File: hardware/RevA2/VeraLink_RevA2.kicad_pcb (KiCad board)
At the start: 2 copper layers, 42 x 42 mm, 55 parts, among them J1 MAG_POGO_3PIN, J2 FACTORY_SWD_PADS, M1 COIN_LRA_MOTOR, SW1 USER_BUTTON, U1 MCP73831-2-OT, U2 TPS78233DDC, U3 nRF52840-QIAA, U4 E22-900M22S_SX1262_LORA, U5 DRV2605LDGS, Y1 32MHz, Y2 32.768 kHZ

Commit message: Apply Rev A2 layout repair pass 2
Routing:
- net Net-(U3-XL2/P0.01): track 3.57 -> 0.00 mm
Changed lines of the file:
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@@
-	)
-	(segment
-		(start 130.5 109.898959)
-		(end 130.5 109.75)
-		(width 0.2)
-		(layer "F.Cu")
-		(net "Net-(U3-XL2{slash}P0.01)")
-	)
-	(segment
-		(start 131.4 112.8)
-		(end 130.325 111.725)
-		(width 0.2)
-		(layer "F.Cu")
-		(net "Net-(U3-XL2{slash}P0.01)")
-	)
-	(segment
-		(start 130.325 111.725)
-		(end 130.325 110.073959)
-		(width 0.2)
-		(layer "F.Cu")
-		(net "Net-(U3-XL2{slash}P0.01)")
-	)
-	(segment
-		(start 130.325 110.073959)
-		(end 130.5 109.898959)
-		(width 0.2)
-		(layer "F.Cu")
-		(net "Net-(U3-XL2{slash}P0.01)")
 	)
 	(segment
@@
 	)
 	(segment
-		(start 130 109.75)
-		(end 129.601041 109.75)
-		(width 0.2)
-		(layer "F.Cu")
-		(net "Net-(U3-XL1{slash}P0.00)")
-	)
-	(segment

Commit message: Set Rev A2 PCB to 4-layer stackup
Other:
- copper layers 2 -> 4
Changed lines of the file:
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@@
 	(layers
 		(0 "F.Cu" signal)
+		(4 "In1.Cu" signal)
+		(6 "In2.Cu" signal)
 		(2 "B.Cu" signal)
 		(9 "F.Adhes" user "F.Adhesive")
@@
 	)
 	(setup
+		(stackup
+			(layer "F.SilkS"
+				(type "Top Silk Screen")
+			)
+			(layer "F.Paste"
+				(type "Top Solder Paste")
+			)
+			(layer "F.Mask"
+				(type "Top Solder Mask")
+				(thickness 0.01)
+			)
+			(layer "F.Cu"
+				(type "copper")
+				(thickness 0.035)
+			)
+			(layer "dielectric 1"
+				(type "prepreg")
+				(thickness 0.1)
+				(material "FR4")
+				(epsilon_r 4.5)
+				(loss_tangent 0.02)
+			)
+			(layer "In1.Cu"
+				(type "copper")
+				(thickness 0.035)
+			)
+			(layer "dielectric 2"
+				(type "core")
+				(thickness 1.24)
+				(material "FR4")
+				(epsilon_r 4.5)
+				(loss_tangent 0.02)
+			)
+			(layer "In2.Cu"
+				(type "copper")
+				(thickness 0.035)
+			)
+			(layer "dielectric 3"
+				(type "prepreg")
+				(thickness 0.1)
+				(material "FR4")
+				(epsilon_r 4.5)
+				(loss_tangent 0.02)
+			)
+			(layer "B.Cu"
+				(type "copper")
+				(thickness 0.035)
+			)
+			(layer "B.Mask"
+				(type "Bottom Solder Mask")
+				(thickness 0.01)
+			)
+			(layer "B.Paste"
+				(type "Bottom Solder Paste")
+			)
+			(layer "B.SilkS"
+				(type "Bottom Silk Screen")
+			)
+			(copper_finish "None")
+			(dielectric_constraints no)
+		)
 		(pad_to_mask_clearance 0)
 		(allow_soldermask_bridges_in_footprints no)
@@
 		(capping no)
 		(filling no)
+		(zone_defaults)
 		(pcbplotparams
 			(layerselection 0x00000000_00000000_55555555_5755f5ff)

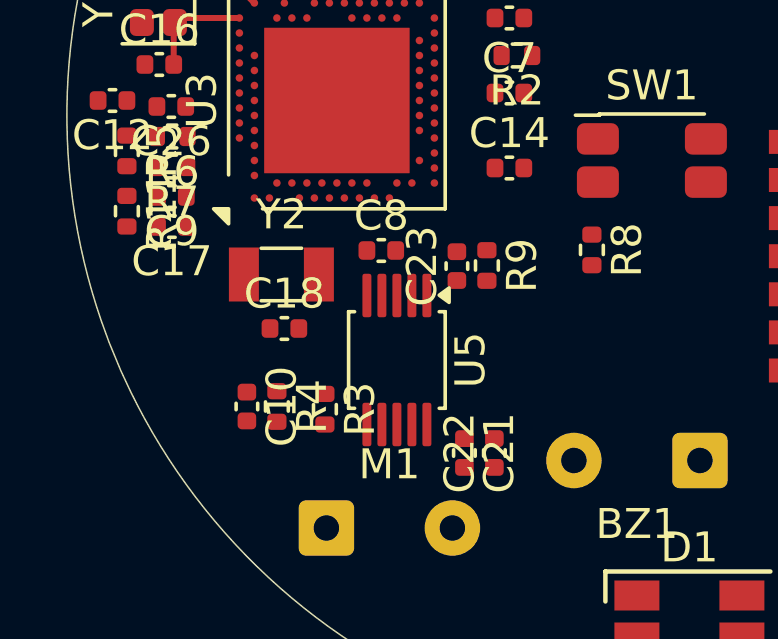
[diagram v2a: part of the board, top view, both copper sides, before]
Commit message: Route Rev A2 low frequency crystal nets
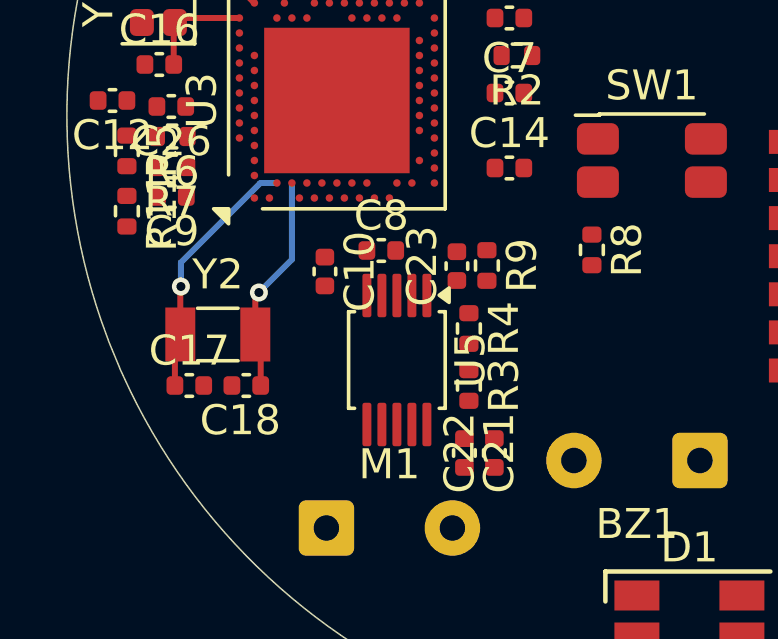
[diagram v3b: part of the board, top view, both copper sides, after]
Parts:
- moved R4 6.91 mm to (136.4, 114.6)
- moved C17 5.33 mm to (127.1, 116.5), turned to 0 degrees
- moved C10 5.20 mm to (131.6, 112.7)
- moved R3 4.86 mm to (136.4, 116.5)
- moved Y2 2.91 mm to (128.0, 114.8)
- moved C18 2.29 mm to (129.0, 116.5), turned to 180 degrees
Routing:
- net Net-(U3-XL1/P0.00): track 0.00 -> 8.48 mm, vias 0 -> 1
- net Net-(U3-XL2/P0.01): track 0.00 -> 7.33 mm, vias 0 -> 1
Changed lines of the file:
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@@
 		(capping no)
 		(filling no)
-		(zone_defaults)
 		(pcbplotparams
 			(layerselection 0x00000000_00000000_55555555_5755f5ff)
@@
 	(footprint "Resistor_SMD:R_0402_1005Metric"
 		(layer "F.Cu")
-		(at 130 117.2 -90)
+		(at 136.4 114.6 -90)
 		(descr "Resistor SMD 0402 (1005 Metric), square (rectangular) end terminal, IPC-7351 nominal, (Body size source: IPC-SM-782 page 72, https://www.pcb-3d.com/wordpress/wp-content/uploads/ipc-sm-782a_amendment_1_and_2.pdf)")
 		(tags "resistor")
@@
 	(footprint "Capacitor_SMD:C_0402_1005Metric"
 		(layer "F.Cu")
-		(at 130.25 114.6)
+		(at 128.98 116.5 180)
 		(descr "Capacitor SMD 0402 (1005 Metric), square (rectangular) end terminal, IPC-7351 nominal, (Body size source: IPC-SM-782 page 76, https://www.pcb-3d.com/wordpress/wp-content/uploads/ipc-sm-782a_amendment_1_and_2.pdf)")
 		(tags "capacitor")
 		(property "Reference" "C18"
-			(at 0 -1.16 0)
+			(at 0.2 -1.16 0)
 			(layer "F.SilkS")
 			(effects
@@
 		(duplicate_pad_numbers_are_jumpers no)
 		(fp_line
-			(start -0.107836 -0.36)
-			(end 0.107836 -0.36)
+			(start -0.107836 0.36)
+			(end 0.107836 0.36)
 			(stroke
 				(width 0.12)
@@
 		)
 		(fp_line
-			(start -0.107836 0.36)
-			(end 0.107836 0.36)
+			(start -0.107836 -0.36)
+			(end 0.107836 -0.36)
 			(stroke
 				(width 0.12)
@@
 		)
 		(pad "1" smd roundrect
-			(at -0.48 0)
+			(at -0.48 0 180)
 			(size 0.56 0.62)
 			(layers "F.Cu" "F.Mask" "F.Paste")
@@
 		)
 		(pad "2" smd roundrect
-			(at 0.48 0)
+			(at 0.48 0 180)
 			(size 0.56 0.62)
 			(layers "F.Cu" "F.Mask" "F.Paste")
@@
 		)
 		(property "Value" "100nF"
-			(at 0 1.16 0)
+			(at -2.12 3.16 0)
 			(layer "F.Fab")
 			(effects
@@
 	(footprint "Capacitor_SMD:C_0402_1005Metric"
 		(layer "F.Cu")
-		(at 129 117.2 -90)
+		(at 131.6 112.7 -90)
 		(descr "Capacitor SMD 0402 (1005 Metric), square (rectangular) end terminal, IPC-7351 nominal, (Body size source: IPC-SM-782 page 76, https://www.pcb-3d.com/wordpress/wp-content/uploads/ipc-sm-782a_amendment_1_and_2.pdf)")
 		(tags "capacitor")
@@
 		)
 		(property "Value" "100nF"
-			(at 0 1.16 270)
+			(at 1.1 1.9 270)
 			(layer "F.Fab")
 			(effects
@@
 	(footprint "Resistor_SMD:R_0402_1005Metric"
 		(layer "F.Cu")
-		(at 131.6 117.29 -90)
+		(at 136.4 116.5 -90)
 		(descr "Resistor SMD 0402 (1005 Metric), square (rectangular) end terminal, IPC-7351 nominal, (Body size source: IPC-SM-782 page 72, https://www.pcb-3d.com/wordpress/wp-content/uploads/ipc-sm-782a_amendment_1_and_2.pdf)")
 		(tags "resistor")
@@
 	(footprint "Crystal:Crystal_SMD_3215-2Pin_3.2x1.5mm"
 		(layer "F.Cu")
-		(at 130.15 112.8)
+		(at 128.03 114.8)
 		(descr "SMD Crystal FC-135 https://support.epson.biz/td/api/doc_check.php?dl=brief_FC-135R_en.pdf")
 		(tags "SMD SMT Crystal")
@@
 	(footprint "Capacitor_SMD:C_0402_1005Metric"
 		(layer "F.Cu")
-		(at 126.5 111.2 180)
+		(at 127.08 116.5)
 		(descr "Capacitor SMD 0402 (1005 Metric), square (rectangular) end terminal, IPC-7351 nominal, (Body size source: IPC-SM-782 page 76, https://www.pcb-3d.com/wordpress/wp-content/uploads/ipc-sm-782a_amendment_1_and_2.pdf)")
 		(tags "capacitor")
 		(property "Reference" "C17"
-			(at 0 -1.16 180)
+			(at 0 -1.16 0)
 			(layer "F.SilkS")
 			(effects
@@
 		)
 		(property "Value" "12.5pF"
-			(at 0 1.16 180)
+			(at 0 1.16 0)
 			(layer "F.Fab")
 			(effects
@@
 		)
 		(property "Datasheet" ""
-			(at 0 0 180)
+			(at 0 0 0)
 			(layer "F.Fab")
 			(hide yes)
@@
 		)
 		(property "Description" "Unpolarized capacitor"
-			(at 0 0 180)
+			(at 0 0 0)
 			(layer "F.Fab")
 			(hide yes)
@@
 		)
 		(property "KiLib_Generator" "SMD_2terminal_chip_molded"
-			(at 0 0 180)
+			(at 0 0 0)
 			(layer "F.SilkS")
 			(hide yes)
@@
 		(duplicate_pad_numbers_are_jumpers no)
 		(fp_line
-			(start -0.107836 0.36)
-			(end 0.107836 0.36)
+			(start -0.107836 -0.36)
+			(end 0.107836 -0.36)
 			(stroke
 				(width 0.12)
@@
 		)
 		(fp_line
-			(start -0.107836 -0.36)
-			(end 0.107836 -0.36)
+			(start -0.107836 0.36)
+			(end 0.107836 0.36)
 			(stroke
 				(width 0.12)
@@
 		)
 		(fp_text user "${REFERENCE}"
-			(at 0 0 180)
+			(at 0 0 0)
 			(layer "F.Fab")
 			(effects
@@
 		)
 		(pad "1" smd roundrect
-			(at -0.48 0 180)
+			(at -0.48 0)
 			(size 0.56 0.62)
 			(layers "F.Cu" "F.Mask" "F.Paste")
@@
 		)
 		(pad "2" smd roundrect
-			(at 0.48 0 180)
+			(at 0.48 0)
 			(size 0.56 0.62)
 			(layers "F.Cu" "F.Mask" "F.Paste")
@@
 	)
 	(segment
+		(start 129.46 116.5)
+		(end 129.46 114.98)
+		(width 0.2)
+		(layer "F.Cu")
+		(net "Net-(U3-XL2{slash}P0.01)")
+	)
+	(segment
+		(start 129.28 114.8)
+		(end 129.28 113.52)
+		(width 0.2)
+		(layer "F.Cu")
+		(net "Net-(U3-XL2{slash}P0.01)")
+	)
+	(segment
+		(start 129.28 113.52)
+		(end 129.4 113.4)
+		(width 0.2)
+		(layer "F.Cu")
+		(net "Net-(U3-XL2{slash}P0.01)")
+	)
+	(segment
+		(start 129.46 114.98)
+		(end 129.28 114.8)
+		(width 0.2)
+		(layer "F.Cu")
+		(net "Net-(U3-XL2{slash}P0.01)")
+	)
+	(via
+		(at 129.4 113.4)
+		(size 0.6)
+		(drill 0.3)
+		(layers "F.Cu" "B.Cu")
+		(net "Net-(U3-XL2{slash}P0.01)")
+	)
+	(segment
+		(start 130.5 112.3)
+		(end 130.5 109.75)
+		(width 0.2)
+		(layer "B.Cu")
+		(net "Net-(U3-XL2{slash}P0.01)")
+	)
+	(segment
+		(start 129.4 113.4)
+		(end 130.5 112.3)
+		(width 0.2)
+		(layer "B.Cu")
+		(net "Net-(U3-XL2{slash}P0.01)")
+	)
+	(segment
 		(start 126.75 104.25)
 		(end 126.6 104.4)
@@
 	)
 	(segment
+		(start 126.6 116.5)
+		(end 126.6 114.98)
+		(width 0.2)
+		(layer "F.Cu")
+		(net "Net-(U3-XL1{slash}P0.00)")
+	)
+	(segment
+		(start 126.6 114.98)
+		(end 126.78 114.8)
+		(width 0.2)
+		(layer "F.Cu")
+		(net "Net-(U3-XL1{slash}P0.00)")
+	)
+	(segment
+		(start 126.78 114.8)
+		(end 126.78 113.22)
+		(width 0.2)
+		(layer "F.Cu")
+		(net "Net-(U3-XL1{slash}P0.00)")
+	)
+	(segment
+		(start 126.78 113.22)
+		(end 126.8 113.2)
+		(width 0.2)
+		(layer "F.Cu")
+		(net "Net-(U3-XL1{slash}P0.00)")
+	)
+	(via
+		(at 126.8 113.2)
+		(size 0.6)
+		(drill 0.3)
+		(layers "F.Cu" "B.Cu")
+		(net "Net-(U3-XL1{slash}P0.00)")
+	)
+	(segment
+		(start 126.8 113.2)
+		(end 126.8 112.4)
+		(width 0.2)
+		(layer "B.Cu")
+		(net "Net-(U3-XL1{slash}P0.00)")
+	)
+	(segment
+		(start 126.8 112.4)
+		(end 129.45 109.75)
+		(width 0.2)
+		(layer "B.Cu")
+		(net "Net-(U3-XL1{slash}P0.00)")
+	)
+	(segment
+		(start 129.45 109.75)
+		(end 130 109.75)
+		(width 0.2)
+		(layer "B.Cu")
+		(net "Net-(U3-XL1{slash}P0.00)")
+	)
+	(segment

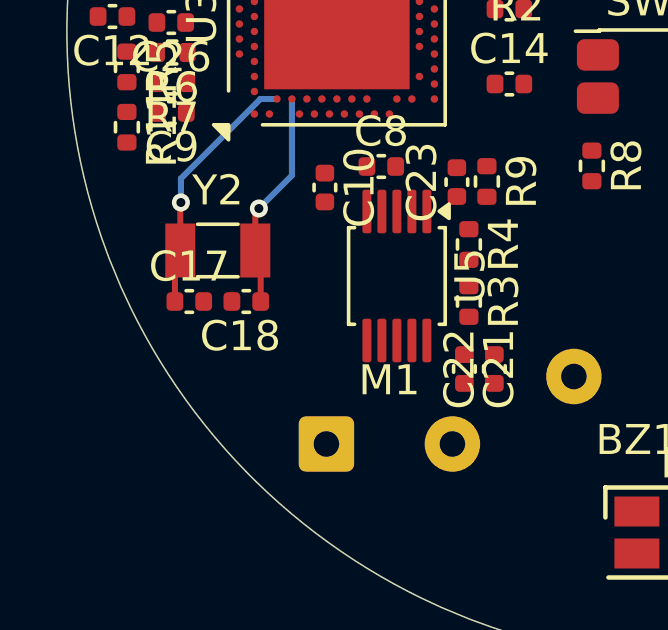
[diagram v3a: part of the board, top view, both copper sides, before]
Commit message: Route Rev A2 low frequency crystal and load capacitor grounds
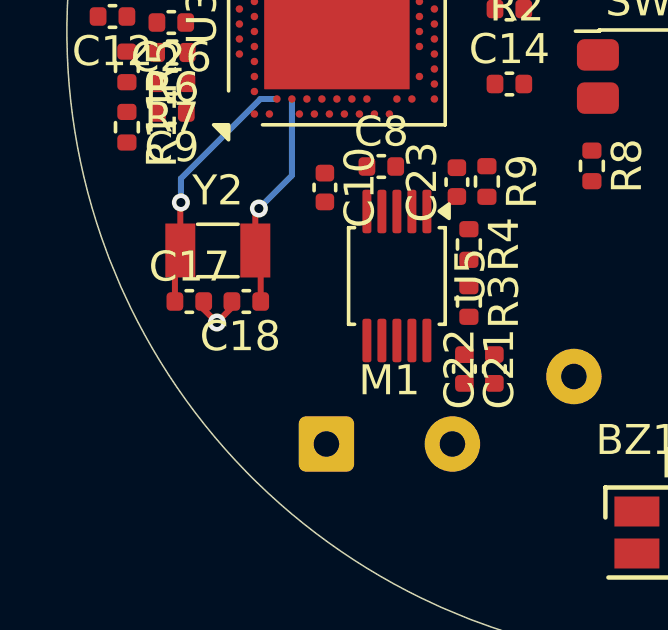
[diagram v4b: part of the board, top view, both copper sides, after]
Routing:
- net GND: track 0.00 -> 1.79 mm, vias 0 -> 1
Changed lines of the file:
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@@
+	)
+	(segment
+		(start 128.5 116.5)
+		(end 128.5 116.7)
+		(width 0.2)
+		(layer "F.Cu")
+		(net "GND")
+	)
+	(segment
+		(start 128.5 116.7)
+		(end 128 117.2)
+		(width 0.2)
+		(layer "F.Cu")
+		(net "GND")
+	)
+	(segment
+		(start 127.56 116.76)
+		(end 128 117.2)
+		(width 0.2)
+		(layer "F.Cu")
+		(net "GND")
+	)
+	(segment
+		(start 127.56 116.5)
+		(end 127.56 116.76)
+		(width 0.2)
+		(layer "F.Cu")
+		(net "GND")
+	)
+	(via
+		(at 128 117.2)
+		(size 0.6)
+		(drill 0.3)
+		(layers "F.Cu" "B.Cu")
+		(net "GND")
 	)
 	(segment

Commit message: Add Rev A2 internal ground plane zone
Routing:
- added copper zone on In1.Cu, net (none)
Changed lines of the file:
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@@
 		(net "/LORA_RF")
+	)
+	(zone
+		(layer "In1.Cu")
+		(name "GND")
+		(hatch edge 0.5)
+		(connect_pads
+			(clearance 0.5)
+		)
+		(min_thickness 0.25)
+		(fill yes
+			(thermal_gap 0.5)
+			(thermal_bridge_width 0.5)
+			(island_removal_mode 1)
+		)
+		(polygon
+			(pts
+				(xy 143.4 128.2) (xy 139 127.6) (xy 130.8 123.4) (xy 126.6 118.6) (xy 123.4 110.2) (xy 124.4 100.4)
+				(xy 127.8 94.4) (xy 135.6 88.4) (xy 141.2 87) (xy 144.8 86.6) (xy 150.4 87.8) (xy 154.6 89.8) (xy 161 95.6)
+				(xy 164.2 102.6) (xy 164.6 109.4) (xy 163.8 114.2) (xy 161.6 118.6) (xy 156.6 124) (xy 152.4 126.6)
+				(xy 147.8 128) (xy 143.6 128.2)
+			)
+		)
 	)
 	(embedded_fonts no)

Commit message: Add Rev A2 local ground vias near U3
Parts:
- moved C12 2.69 mm to (126.5, 108.8)
- moved C9 0.80 mm to (126.5, 111.0)
- moved R7 0.80 mm to (126.5, 110.0)
- moved C24 0.50 mm to (134.0, 100.0)
- moved R6 0.40 mm to (126.5, 107.8)
- moved C26 0.40 mm to (126.5, 106.8)
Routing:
- net GND: track 1.79 -> 7.46 mm, vias 1 -> 6
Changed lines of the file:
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@@
 	(footprint "Capacitor_SMD:C_0402_1005Metric"
 		(layer "F.Cu")
-		(at 124.52 107 180)
+		(at 126.52 108.8 180)
 		(descr "Capacitor SMD 0402 (1005 Metric), square (rectangular) end terminal, IPC-7351 nominal, (Body size source: IPC-SM-782 page 76, https://www.pcb-3d.com/wordpress/wp-content/uploads/ipc-sm-782a_amendment_1_and_2.pdf)")
 		(tags "capacitor")
@@
 	(footprint "Capacitor_SMD:C_0402_1005Metric"
 		(layer "F.Cu")
-		(at 126.5 110.2 180)
+		(at 126.52 111 180)
 		(descr "Capacitor SMD 0402 (1005 Metric), square (rectangular) end terminal, IPC-7351 nominal, (Body size source: IPC-SM-782 page 76, https://www.pcb-3d.com/wordpress/wp-content/uploads/ipc-sm-782a_amendment_1_and_2.pdf)")
 		(tags "capacitor")
@@
 	(footprint "Capacitor_SMD:C_0402_1005Metric"
 		(layer "F.Cu")
-		(at 134.5 100)
+		(at 134 100)
 		(descr "Capacitor SMD 0402 (1005 Metric), square (rectangular) end terminal, IPC-7351 nominal, (Body size source: IPC-SM-782 page 76, https://www.pcb-3d.com/wordpress/wp-content/uploads/ipc-sm-782a_amendment_1_and_2.pdf)")
 		(tags "capacitor")
@@
 	(footprint "Capacitor_SMD:C_0402_1005Metric"
 		(layer "F.Cu")
-		(at 126.48 107.2 180)
+		(at 126.48 106.8 180)
 		(descr "Capacitor SMD 0402 (1005 Metric), square (rectangular) end terminal, IPC-7351 nominal, (Body size source: IPC-SM-782 page 76, https://www.pcb-3d.com/wordpress/wp-content/uploads/ipc-sm-782a_amendment_1_and_2.pdf)")
 		(tags "capacitor")
@@
 	(footprint "Resistor_SMD:R_0402_1005Metric"
 		(layer "F.Cu")
-		(at 126.5 109.2 180)
+		(at 126.5 110 180)
 		(descr "Resistor SMD 0402 (1005 Metric), square (rectangular) end terminal, IPC-7351 nominal, (Body size source: IPC-SM-782 page 72, https://www.pcb-3d.com/wordpress/wp-content/uploads/ipc-sm-782a_amendment_1_and_2.pdf)")
 		(tags "resistor")
@@
 	(footprint "Resistor_SMD:R_0402_1005Metric"
 		(layer "F.Cu")
-		(at 126.51 108.2 180)
+		(at 126.49 107.8 180)
 		(descr "Resistor SMD 0402 (1005 Metric), square (rectangular) end terminal, IPC-7351 nominal, (Body size source: IPC-SM-782 page 72, https://www.pcb-3d.com/wordpress/wp-content/uploads/ipc-sm-782a_amendment_1_and_2.pdf)")
 		(tags "resistor")
@@
 	)
 	(segment
+		(start 130.75 100.77)
+		(end 131.57 100.77)
+		(width 0.2)
+		(layer "F.Cu")
+		(net "GND")
+	)
+	(segment
+		(start 125.72 101.6)
+		(end 125 101.6)
+		(width 0.2)
+		(layer "F.Cu")
+		(net "GND")
+	)
+	(segment
+		(start 129.75 100.05)
+		(end 129.8 100)
+		(width 0.2)
+		(layer "F.Cu")
+		(net "GND")
+	)
+	(segment
 		(start 128.5 116.5)
 		(end 128.5 116.7)
@@
 	)
 	(segment
+		(start 126.04 111)
+		(end 126.04 111.36)
+		(width 0.2)
+		(layer "F.Cu")
+		(net "GND")
+	)
+	(segment
+		(start 131.63 100.77)
+		(end 131.6 100.8)
+		(width 0.2)
+		(layer "F.Cu")
+		(net "GND")
+	)
+	(segment
+		(start 125.6 105.8)
+		(end 124.8 105.8)
+		(width 0.2)
+		(layer "F.Cu")
+		(net "GND")
+	)
+	(segment
 		(start 127.56 116.76)
 		(end 128 117.2)
@@
 	)
 	(segment
+		(start 126.04 111.36)
+		(end 125.6 111.8)
+		(width 0.2)
+		(layer "F.Cu")
+		(net "GND")
+	)
+	(segment
+		(start 132.25 100.77)
+		(end 131.63 100.77)
+		(width 0.2)
+		(layer "F.Cu")
+		(net "GND")
+	)
+	(segment
+		(start 125 111.2)
+		(end 125.6 111.8)
+		(width 0.2)
+		(layer "F.Cu")
+		(net "GND")
+	)
+	(segment
+		(start 129.75 100.77)
+		(end 129.75 100.05)
+		(width 0.2)
+		(layer "F.Cu")
+		(net "GND")
+	)
+	(segment
+		(start 131.57 100.77)
+		(end 131.6 100.8)
+		(width 0.2)
+		(layer "F.Cu")
+		(net "GND")
+	)
+	(segment
 		(start 127.56 116.5)
 		(end 127.56 116.76)
@@
 	)
 	(via
+		(at 125 101.6)
+		(size 0.6)
+		(drill 0.3)
+		(layers "F.Cu" "B.Cu")
+		(net "GND")
+	)
+	(via
 		(at 128 117.2)
 		(size 0.6)
 		(drill 0.3)
+		(layers "F.Cu" "B.Cu")
+		(net "GND")
+	)
+	(via
+		(at 124.8 105.8)
+		(size 0.6)
+		(drill 0.3)
+		(layers "F.Cu" "B.Cu")
+		(net "GND")
+	)
+	(via
+		(at 125.6 111.8)
+		(size 0.6)
+		(drill 0.3)
+		(layers "F.Cu" "B.Cu")
+		(net "GND")
+	)
+	(via
+		(at 129.8 100)
+		(size 0.6)
+		(drill 0.3)
+		(layers "F.Cu" "B.Cu")
+		(net "GND")
+	)
+	(via
+		(at 131.6 100.8)
+		(size 0.6)
+		(drill 0.3)
